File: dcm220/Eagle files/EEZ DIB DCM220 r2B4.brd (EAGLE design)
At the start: 155 x 95 mm, 248 parts, among them IC1 Si8662AB-B-IS1, IC10 MC33272ADR2G, IC11 LT3763EFE#PBF, IC12 MC33274ADR2G, IC13 LT3763EFE#PBF, IC2 TPS54060DGQ, IC3 Si8641AB-B-IS1, IC4 M24C32-WMN6P, IC5 LP2985-33DBVR, IC6 74HC2G04GW,125, IC7 N.C., IC8 STM32F373C8T6, IC9 TL431B, J1 4907, J2 571-0500, J3 571-0100, J4 571-0500, J5 571-0100, Q1 BSP716NH6327XTSA1, Q10 BSS84, Q2 NTD5867NLT4G, Q3 NTD5867NLT4G, Q4 BSS205NH6327XTSA1, Q5 BSS84, Q6 BSP716NH6327XTSA1, Q7 NTD5867NLT4G, Q8 NTD5867NLT4G, Q9 BSS205NH6327XTSA1, X1 172648-0102, X2 77317-104-28LF, X3 N.C., X4 DS1024-2*5R0, Y1 LF XTAL026392

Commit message: DCM220 r2B4
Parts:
- removed R76: 3K6, rcl:R0805
- removed R77: 120R, rcl:R0805
- removed R78: 11K8, rcl:R0805
- removed R79: 15K, rcl:R0805
- added D10: N.C., EEZ_Lib1:SOD123
- added D11, D9: SKL16, EEZ_Lib1:SOD123
- added D12: N.C., EEZ_Lib1:SMA
- C13: value 22u -> N.C.
- C16: value 18p -> 33p
- C22: value 1u -> N.C.
- C55, C75: device rcl:C1210 -> rcl:C1206
- D3, D4, D6: value BAW56L -> SKL16; device EEZ_Lib1:SOT23 -> EEZ_Lib1:SOD123
- D5: device EEZ_Lib1:SMA -> EEZ_Lib1:SOD123
- D7: value BAW56L -> N.C.; device EEZ_Lib1:SOT23 -> EEZ_Lib1:SMA
- D8: value N.C. -> SKL16; device EEZ_Lib1:SMA -> EEZ_Lib1:SOD123
- KK1, KK2: value PCB-MB -> PMB-1
- R29: value 330K -> 86K6
- R30, R56: value 22K -> 16K
- R32: value 0R -> 16K
- R33: value 22K -> 10K
- R34: value 10K -> R012/2W; device rcl:R0805 -> EEZ_Lib1:R_2512-4WIRE
- R35: value R012/2W -> 10R; device EEZ_Lib1:R_2512-4WIRE -> rcl:R0805
- R37: value 10R -> N.C.; device rcl:R0805 -> rcl:R1206
- R38: value 0R -> 2K2
- R39: value N.C. -> 30K; device rcl:R1206 -> rcl:R0805
- R40, R66: value 2K2 -> 86K6
- R41: value 30K -> 3K3
- R43: value 3K3 -> 47K
- R44, R68: value 86K6 -> 47K
- R45: value 47K -> 30K
- R46: value 47K -> 3K9
- R47: value 30K -> 12K
- R48: value 3K9 -> 3K6
- R49: value 12K -> 120R
- R50: value 3K6 -> 11K8
- R51: value 120R -> 15K
- R52: value 11K8 -> 10R
- R53: value 15K -> 86K6
- R54: value 10R -> 16K
- R55: value 330K -> 10K
- R58: value 0R -> R012/2W; device rcl:R0805 -> EEZ_Lib1:R_2512-4WIRE
- R59: value 22K -> 10R
- R60: value 10K -> 10R
- R61: value R012/2W -> N.C.; device EEZ_Lib1:R_2512-4WIRE -> rcl:R1206
- R62: value 10R -> 2K2
- R63: value 10R -> 30K
- R64: value 0R -> 86K6
- R65: value N.C. -> 3K3; device rcl:R1206 -> rcl:R0805
- R67: value 30K -> 47K
- R69: value 3K3 -> 30K
- R70: value 86K6 -> 3K9
- R71: value 47K -> 12K
- R72: value 47K -> 3K6
- R73: value 30K -> 120R
- R74: value 3K9 -> 11K8
- R75: value 12K -> 15K
- X1: value 172648-0102 -> 39-30-1020
- ZD2, ZD4: value MM3Z9V1T1G -> MM3Z2V4T1G
- moved R51 97.0 mm to (124.9, 73.2), turned to 180 degrees
- moved R69 72.5 mm to (85.3, 39.8), turned to 0 degrees
- moved R41 71.8 mm to (13.7, 66.4)
- moved R73 65.3 mm to (25.6, 13.3)
- moved R43 65.3 mm to (76.1, 85.5)
- moved R49 64.0 mm to (29.7, 54.3), turned to 90 degrees
- moved R74 53.9 mm to (124.9, 67.4), turned to 0 degrees
- moved R34 52.0 mm to (39.9, 78.5)
- moved D8 51.8 mm to (94.5, 53.5), turned to 270 degrees
- moved D5 49.8 mm to (94.3, 86.6), turned to 0 degrees
- moved R75 49.0 mm to (124.9, 69.4), turned to 180 degrees
- moved R59 44.9 mm to (46.0, 38.7), turned to 180 degrees
- moved R60 42.4 mm to (46.0, 40.8), turned to 180 degrees
- moved R63 40.1 mm to (85.3, 33.0), turned to 270 degrees
- moved D6 38.1 mm to (70.8, 84.5)
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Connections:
- removed net N$19: Q2.1, R32.2
- removed net N$2: Q3.1, R38.2
- removed net N$256: Q7.1, R58.2
- removed net N$258: Q8.1, R64.2
- net +8V: now also D10.A, D5.A
- net CC_LED#1: now also R49.2; no longer R51.2
- net CC_LED#2: now also R73.2; no longer R77.2
- net DC_OUT+: now also R52.1, R53.1; no longer R54.1, R55.1
- net DC_OUT-: now also D12.A, D7.A, R37.1, R41.2, R61.1, R65.2; no longer D5.A, D8.A, R39.1, R43.2, R65.1, R69.2
- net FB1: now also R39.1, R46.2; no longer R41.1, R50.2
- net FB2: now also R63.1, R70.2, R72.2; no longer R67.1, R74.2, R76.2
- net GND: now also R33.1, R42.1, R45.1, R46.1, R51.1, R54.1, R57.1, R66.1, R69.1, R71.1; no longer R34.1, R44.1, R48.1, R49.1, R53.1, R56.1, R60.1, R73.1, R74.1, R79.1
- net INTVCC1: now also D6.A, R43.1, R44.2; no longer D4.3, R45.1, R46.2
- net INTVCC2: now also D11.A, R67.1, R68.2; no longer D7.3, R71.1, R72.2
- net ISET2: now also R55.2; no longer R57.2
- net I_MON1: now also R38.1; no longer R40.1
- net I_MON2: now also R62.1; no longer R66.1
- net I_SET#1: now also R32.1; no longer R33.1
- net I_SET#2: now also R56.1; no longer R59.1
- net LOUT1: now also R34.1; no longer R35.1
- net LOUT2: now also R58.1; no longer R61.1
- net N$1: now also Q3.1; no longer R38.1
- net N$11: now also R49.1; no longer R51.1
- net N$13: now also R45.2; no longer R47.2
- net N$15: now also Q2.1; no longer R32.1
- net N$16: now also R34.2S, R36.2; no longer R35.2S, R37.2
- net N$17: now also R37.2; no longer R39.2
- net N$18: now also R44.1; no longer R46.1
- net N$22: now also D6.C; no longer D4.1, D4.2
- net N$25: now also R73.1; no longer R77.1
- net N$250: now also R32.2; no longer R34.2
- net N$253: now also R68.1; no longer R72.1
- net N$255: now also Q7.1; no longer R58.1
- net N$257: now also Q8.1; no longer R64.1
- net N$26: now also D4.C; no longer D3.1
- net N$261: now also R58.1S, R59.2; no longer R61.1S, R62.2
- net N$262: now also R58.2S, R60.2; no longer R61.2S, R63.2
- net N$263: now also R61.2; no longer R65.2
- net N$264: now also D11.C; no longer D7.1, D7.2
- net N$267: now also R62.2; no longer R66.2
- net N$271: now also R74.1, R75.2; no longer R78.1, R79.2
- net N$278: now also R54.2, R55.1; no longer R56.2, R57.1
- net N$28: now also R66.2; no longer R70.2
- net N$311: now also R56.2, R57.2; no longer R59.2, R60.2
- net N$37: now also R69.2; no longer R73.2
- net N$39: now also D3.C, D5.C; no longer D3.2
- net N$42: now also D10.C, D8.C; no longer D6.2
- net N$43: now also D3.A, D4.A; no longer D3.3
- net N$46: now also D9.C, R53.2; no longer D6.1, R55.2
- net N$48: now also R38.2; no longer R40.2
- net N$54: now also R50.1, R51.2; no longer R52.1, R53.2
- net N$61: now also D8.A, D9.A; no longer D6.3
- net N$7: now also R34.1S, R35.2; no longer R35.1S, R36.2
- net N$8: now also R42.2; no longer R44.2
- net PWM#1: now also R43.2; no longer R45.2
- net PWM#2: now also R67.2; no longer R71.2
- net Q6D: now also R52.2; no longer R54.2
- net SENSE1+: now also R35.1; no longer R36.1
- net SENSE1+1: now also R59.1; no longer R62.1
- net SENSE1-: now also R36.1; no longer R37.1
- net SENSE1-1: now also R60.1; no longer R63.1
- net SW1: now also D7.C; no longer D5.C
- net SW2: now also D12.C; no longer D8.C
- net U_MON1: now also R40.1, R47.2; no longer R42.1, R49.2
- net U_MON2: now also R64.1, R71.2; no longer R68.1, R75.2
- net U_SET#1: now also R48.1; no longer R50.1
- net U_SET#2: now also R72.1; no longer R76.1
- net VOUT1+: now also R34.2, R39.2, R40.2; no longer R35.2, R41.2, R42.2
- net VOUT2+: now also R58.2, R63.2, R64.2; no longer R61.2, R67.2, R68.2
- net VOUT_LC1+: now also R41.1; no longer R43.1
- net VOUT_LC2+: now also R65.1; no longer R69.1
- net VREF1: now also R50.2; no longer R52.2
- net VREF2: now also R74.2; no longer R78.2
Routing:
- net +8V: track 89.9 -> 124.0 mm, vias 2 -> 6
- net N$257: track 3.88 -> 19.9 mm, vias 0 -> 2
- net N$1: track 3.42 -> 19.4 mm, vias 0 -> 2
- net N$15: track 13.6 -> 28.2 mm
- net N$2: track 14.3 -> 0.00 mm, vias 2 -> 0
- net N$258: track 14.0 -> 0.00 mm, vias 2 -> 0
- net N$255: track 13.5 -> 27.4 mm
- net N$19: track 12.5 -> 0.00 mm
- net N$256: track 11.7 -> 0.00 mm
- net N$39: track 36.2 -> 42.7 mm
- net N$42: track 42.7 -> 47.2 mm
- net I_MON2: track 46.2 -> 43.9 mm
- net N$22: track 8.19 -> 6.30 mm
- net Q6D: track 1.84 -> 0.00 mm
- net N$264: track 8.27 -> 6.54 mm
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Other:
- board text added: "EEZ DIB DCM220 (10/2019 r2B4)"
- board text added: "EEZ DIB DCM220 (10/2019 r2B4) Project source code: github.com/eez-open"
- board text removed: "EEZ DIB DCM220 (10/2019 r2B3)"
- board text removed: "EEZ DIB DCM220 (10/2019 r2B3) Project source code: github.com/eez-open"

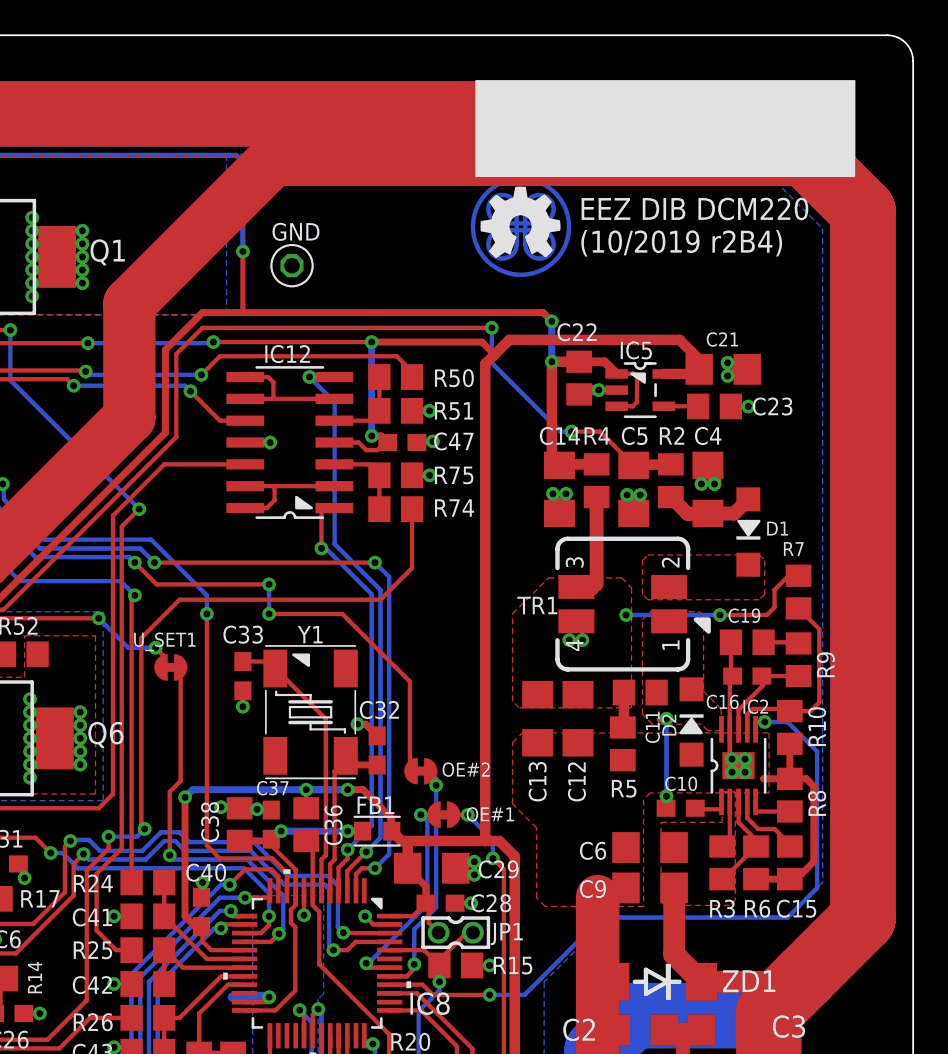
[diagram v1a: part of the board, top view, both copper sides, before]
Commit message: DCM220 eagle files
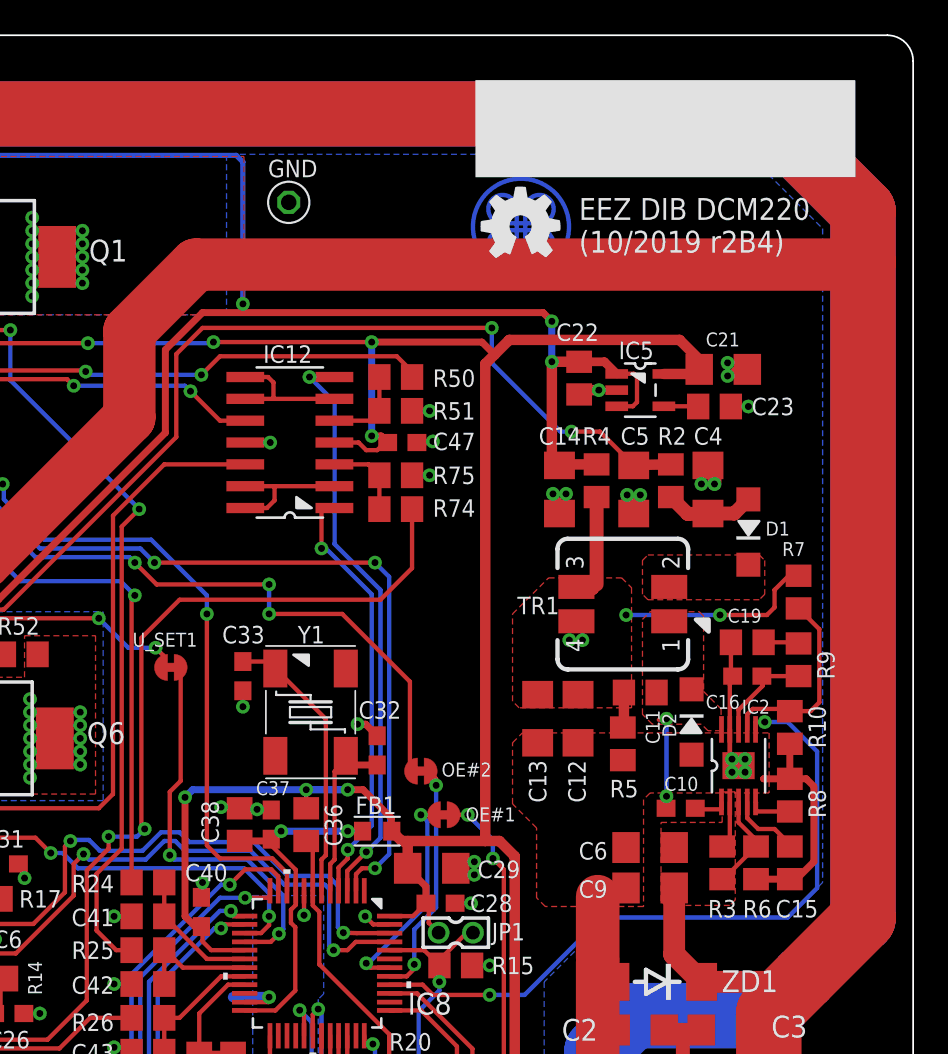
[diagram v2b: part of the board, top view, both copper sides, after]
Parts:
- R30, R32, R54, R56: value 16K -> 22K
- moved GND 3.69 mm to (118.7, 85.3)
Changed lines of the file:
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@@
 <grid distance="2.5" unitdist="mil" unit="mil" style="lines" multiple="10" display="no" altdistance="2.5" altunitdist="mil" altunit="mil"/>
 <layers>
-<layer number="1" name="Top" color="3" fill="1" visible="no" active="yes"/>
+<layer number="1" name="Top" color="3" fill="1" visible="yes" active="yes"/>
 <layer number="2" name="Route2" color="1" fill="3" visible="no" active="no"/>
 <layer number="3" name="Route3" color="4" fill="3" visible="no" active="no"/>
@@
 <layer number="14" name="Route14" color="1" fill="6" visible="no" active="no"/>
 <layer number="15" name="Route15" color="4" fill="6" visible="no" active="no"/>
-<layer number="16" name="Bottom" color="1" fill="1" visible="no" active="yes"/>
-<layer number="17" name="Pads" color="14" fill="1" visible="no" active="yes"/>
-<layer number="18" name="Vias" color="6" fill="1" visible="no" active="yes"/>
-<layer number="19" name="Unrouted" color="6" fill="1" visible="no" active="yes"/>
+<layer number="16" name="Bottom" color="1" fill="1" visible="yes" active="yes"/>
+<layer number="17" name="Pads" color="14" fill="1" visible="yes" active="yes"/>
+<layer number="18" name="Vias" color="6" fill="1" visible="yes" active="yes"/>
+<layer number="19" name="Unrouted" color="6" fill="1" visible="yes" active="yes"/>
 <layer number="20" name="Dimension" color="4" fill="1" visible="yes" active="yes"/>
 <layer number="21" name="tPlace" color="7" fill="1" visible="yes" active="yes"/>
 <layer number="22" name="bPlace" color="6" fill="1" visible="no" active="yes"/>
-<layer number="23" name="tOrigins" color="15" fill="1" visible="no" active="yes"/>
+<layer number="23" name="tOrigins" color="15" fill="1" visible="yes" active="yes"/>
 <layer number="24" name="bOrigins" color="15" fill="1" visible="no" active="yes"/>
 <layer number="25" name="tNames" color="7" fill="1" visible="yes" active="yes"/>
 <layer number="26" name="bNames" color="5" fill="1" visible="no" active="yes"/>
-<layer number="27" name="tValues" color="10" fill="1" visible="yes" active="yes"/>
+<layer number="27" name="tValues" color="10" fill="1" visible="no" active="yes"/>
 <layer number="28" name="bValues" color="10" fill="1" visible="no" active="yes"/>
 <layer number="29" name="tStop" color="7" fill="1" visible="yes" active="yes"/>
@@
 <attribute name="VALUE" x="81.5975" y="58.42" size="1.016" layer="27" ratio="10"/>
 </element>
-<element name="R30" library="rcl" package="R0805" value="16K" x="86.741" y="58.9915" smashed="yes" rot="R180">
+<element name="R30" library="rcl" package="R0805" value="22K" x="86.741" y="58.9915" smashed="yes" rot="R180">
 <attribute name="NAME" x="85.4075" y="60.1345" size="1.016" layer="25" ratio="10"/>
 <attribute name="VALUE" x="85.598" y="58.4835" size="1.016" layer="27" ratio="10"/>
@@
 <attribute name="VALUE" x="78.994" y="50.2285" size="1.016" layer="27" ratio="10" rot="R90"/>
 </element>
-<element name="R54" library="rcl" package="R0805" value="16K" x="74.549" y="51.4985" smashed="yes" rot="R90">
+<element name="R54" library="rcl" package="R0805" value="22K" x="74.549" y="51.4985" smashed="yes" rot="R90">
 <attribute name="NAME" x="74.8665" y="53.594" size="0.8128" layer="25" ratio="10" rot="R90"/>
 <attribute name="VALUE" x="74.041" y="52.959" size="1.016" layer="27" ratio="10" rot="R270"/>
@@
 <attribute name="VALUE" x="87.4395" y="54.864" size="1.016" layer="27" ratio="10" rot="R90"/>
 </element>
-<element name="R32" library="rcl" package="R0805" value="16K" x="88.8365" y="56.007" smashed="yes" rot="R90">
+<element name="R32" library="rcl" package="R0805" value="22K" x="88.8365" y="56.007" smashed="yes" rot="R90">
 <attribute name="NAME" x="89.916" y="58.166" size="0.8128" layer="25" ratio="10" rot="R90"/>
 <attribute name="VALUE" x="89.281" y="54.737" size="1.016" layer="27" ratio="10" rot="R90"/>
@@
 <attribute name="VALUE" x="87.249" y="50.8635" size="1.016" layer="27" ratio="10" rot="R90"/>
 </element>
-<element name="R56" library="rcl" package="R0805" value="16K" x="88.8365" y="52.07" smashed="yes" rot="R270">
+<element name="R56" library="rcl" package="R0805" value="22K" x="88.8365" y="52.07" smashed="yes" rot="R270">
 <attribute name="NAME" x="87.8205" y="49.149" size="0.8128" layer="25" ratio="10"/>
 <attribute name="VALUE" x="89.281" y="50.927" size="1.016" layer="27" ratio="10" rot="R90"/>
 </element>
-<element name="GND" library="EEZ_connectors" package="TEST-PIN_0.9MM" value="" x="118.872" y="81.5975" smashed="yes">
-<attribute name="NAME" x="117.6655" y="83.058" size="1.016" layer="25" ratio="10"/>
+<element name="GND" library="EEZ_connectors" package="TEST-PIN_0.9MM" value="" x="118.6815" y="85.2805" smashed="yes">
+<attribute name="NAME" x="117.475" y="86.741" size="1.016" layer="25" ratio="10"/>
 </element>
 <element name="SH1" library="EEZ_Lib1" package="SHORT_NOHOLE" value="" x="136.652" y="41.2115" smashed="yes" rot="MR0"/>
@@
 <vertex x="59.309" y="36.6395"/>
 </polygon>
-<wire x1="117.7925" y1="87.757" x2="149.098" y2="87.757" width="3.048" layer="1"/>
-<wire x1="152.0825" y1="43.6245" x2="152.0825" y2="84.7725" width="3.81" layer="1"/>
+<wire x1="113.284" y1="81.661" x2="151.9555" y2="81.661" width="3.048" layer="1"/>
+<wire x1="152.0825" y1="43.6245" x2="152.0825" y2="81.788" width="3.81" layer="1"/>
+<wire x1="152.0825" y1="81.788" x2="152.0825" y2="84.7725" width="3.81" layer="1"/>
 <wire x1="146.605" y1="33.5985" x2="146.605" y2="37.2745" width="3.81" layer="1"/>
 <wire x1="146.605" y1="37.2745" x2="146.605" y2="38.147" width="3.81" layer="1"/>
 <wire x1="146.605" y1="38.147" x2="148.6535" y2="40.1955" width="3.81" layer="1"/>
 <wire x1="148.6535" y1="40.1955" x2="152.0825" y2="43.6245" width="3.81" layer="1"/>
-<wire x1="146.431" y1="90.424" x2="149.098" y2="87.757" width="3.81" layer="1"/>
-<wire x1="149.098" y1="87.757" x2="152.0825" y2="84.7725" width="3.81" layer="1"/>
 <wire x1="78.1685" y1="64.3255" x2="64.643" y2="50.8" width="3.048" layer="1"/>
 <wire x1="145.4815" y1="37.1475" x2="146.478" y2="37.1475" width="0.254" layer="1"/>
@@
 <wire x1="73.0885" y1="38.0365" x2="74.422" y2="38.0365" width="0.254" layer="16"/>
 <wire x1="74.422" y1="38.0365" x2="74.93" y2="37.5285" width="0.254" layer="1"/>
-<wire x1="109.4105" y1="79.375" x2="117.7925" y2="87.757" width="3.048" layer="1"/>
 <wire x1="98.9965" y1="88.834" x2="98.9965" y2="90.297" width="0.6096" layer="1"/>
 <wire x1="98.9965" y1="90.297" x2="99.1235" y2="90.424" width="0.6096" layer="1"/>
@@
 <wire x1="78.1685" y1="64.3255" x2="100.965" y2="64.3255" width="3.048" layer="1"/>
 <wire x1="100.965" y1="64.3255" x2="109.4105" y2="72.771" width="3.048" layer="1"/>
-<wire x1="109.4105" y1="72.771" x2="109.4105" y2="79.375" width="3.048" layer="1"/>
 <wire x1="100.137" y1="58.9915" x2="100.137" y2="59.3065" width="0.4064" layer="1"/>
 <wire x1="100.137" y1="59.3065" x2="100.1395" y2="60.2615" width="0.4064" layer="1"/>
@@
 <wire x1="100.965" y1="63.5" x2="100.1395" y2="63.246" width="0.4064" layer="1"/>
 <wire x1="100.137" y1="58.9915" x2="102.174" y2="58.9915" width="0.4064" layer="1"/>
+<wire x1="113.284" y1="81.661" x2="109.4105" y2="77.7875" width="3.048" layer="1"/>
+<wire x1="109.4105" y1="72.771" x2="109.4105" y2="77.7875" width="3.048" layer="1"/>
+<wire x1="146.431" y1="90.424" x2="152.0825" y2="84.7725" width="3.81" layer="1"/>
+<wire x1="151.9555" y1="81.661" x2="152.0825" y2="81.788" width="3.048" layer="1"/>
 </signal>
 <signal name="DC-">
@@
 <via x="96.2025" y="87.6935" extent="1-16" drill="0.4" shape="octagon"/>
 <wire x1="96.52" y1="88.011" x2="115.6335" y2="88.011" width="0.3048" layer="16"/>
-<via x="116.0145" y="82.423" extent="1-16" drill="0.4" shape="octagon"/>
-<wire x1="116.0145" y1="82.423" x2="116.0145" y2="78.994" width="0.3048" layer="1"/>
+<via x="116.0145" y="79.375" extent="1-16" drill="0.4" shape="octagon"/>
+<wire x1="116.0145" y1="79.375" x2="116.0145" y2="78.994" width="0.3048" layer="1"/>
 <wire x1="116.0145" y1="78.994" x2="115.8875" y2="78.867" width="0.3048" layer="1"/>
 <wire x1="115.6335" y1="88.011" x2="116.0145" y2="87.63" width="0.3048" layer="16"/>
-<wire x1="116.0145" y1="87.63" x2="116.0145" y2="82.423" width="0.3048" layer="16"/>
+<wire x1="116.0145" y1="87.63" x2="116.0145" y2="79.375" width="0.3048" layer="16"/>
 <wire x1="96.52" y1="88.011" x2="96.2025" y2="87.6935" width="0.3048" layer="16"/>
 <wire x1="96.1975" y1="86.614" x2="96.1975" y2="87.6885" width="0.3048" layer="1"/>
